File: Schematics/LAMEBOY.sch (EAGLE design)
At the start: 58 parts, among them IC1 PCF8574T, IC3 MCP73831, Q1 12MHz, U1 USD-SOCKETMICROSDEBAY, U2 USB

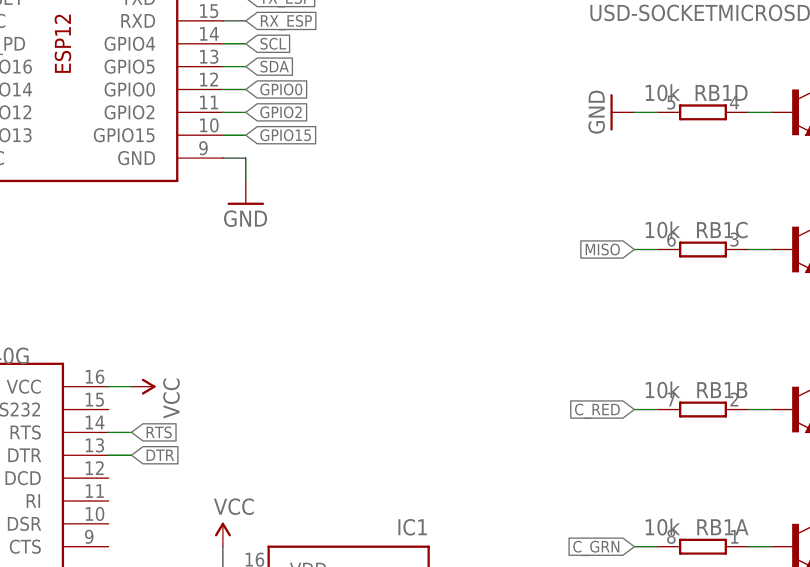
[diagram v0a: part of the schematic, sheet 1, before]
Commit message: bigger better resistor and crystal footprint
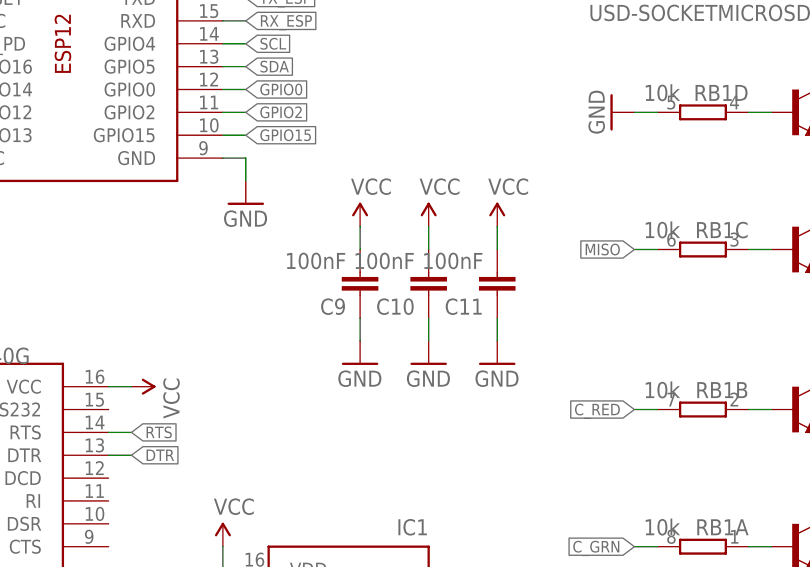
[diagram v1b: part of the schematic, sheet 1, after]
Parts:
- added C10, C11, C9: 100nF, rcl:C-EUONEFITSALL
- C1, C2, C3, C4, C5, C6, C7, C8: device rcl:C-EUC0603K -> rcl:C-EUONEFITSALL
- Q1: device adafruit:XTAL-4-3225 -> adafruit:XTAL-4BIGGER
- R1, R10, R11, R12, R13, R2, R3, R4, R5, R6, R7, R8, R9: device rcl:R-EU_R0603 -> rcl:R-EU_ONEFITSALL
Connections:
- net VREG_OUT renamed VREG_EN
- net GND: now also C10.1, C11.1, C9.1
- net VCC: now also C10.2, C11.2, C9.2
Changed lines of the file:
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@@
 <parts>
 <part name="U$1" library="lph-7366" deviceset="LPH-7366-SLOTS" device=""/>
-<part name="C1" library="rcl" deviceset="C-EU" device="C0603K" value="1uF"/>
+<part name="C1" library="rcl" deviceset="C-EU" device="ONEFITSALL" value="1uF"/>
 <part name="GND1" library="supply1" deviceset="GND" device=""/>
 <part name="LED1" library="led" deviceset="GM1WA55311A" device=""/>
@@
 <part name="LED3" library="led" deviceset="GM1WA55311A" device=""/>
 <part name="LED4" library="led" deviceset="GM1WA55311A" device=""/>
-<part name="C2" library="rcl" deviceset="C-EU" device="C0603K" value="1uF"/>
-<part name="C3" library="rcl" deviceset="C-EU" device="C0603K" value="1uF"/>
-<part name="C4" library="rcl" deviceset="C-EU" device="C0603K" value="1uF"/>
+<part name="C2" library="rcl" deviceset="C-EU" device="ONEFITSALL" value="1uF"/>
+<part name="C3" library="rcl" deviceset="C-EU" device="ONEFITSALL" value="1uF"/>
+<part name="C4" library="rcl" deviceset="C-EU" device="ONEFITSALL" value="1uF"/>
 <part name="GND2" library="supply1" deviceset="GND" device=""/>
 <part name="X1" library="adafruit" deviceset="ESP-12" device=""/>
@@
 <part name="SUPPLY3" library="SparkFun-Aesthetics" deviceset="VCC" device=""/>
 <part name="GND5" library="supply1" deviceset="GND" device=""/>
-<part name="R1" library="rcl" deviceset="R-EU_" device="R0603" value="10k"/>
+<part name="R1" library="rcl" deviceset="R-EU_" device="ONEFITSALL" value="10k"/>
 <part name="CH340G" library="ch340g" deviceset="CH340G" device="CH340G"/>
 <part name="IC1" library="micro-philips" deviceset="PCF8574" device="T" value="PCF8574T"/>
@@
 <part name="GND10" library="supply1" deviceset="GND" device=""/>
 <part name="GND11" library="supply1" deviceset="GND" device=""/>
-<part name="Q1" library="adafruit" deviceset="XTAL-4" device="-3225" value="12MHz"/>
-<part name="C5" library="rcl" deviceset="C-EU" device="C0603K" value="22pF"/>
-<part name="C6" library="rcl" deviceset="C-EU" device="C0603K" value="22pF"/>
-<part name="R2" library="rcl" deviceset="R-EU_" device="R0603" value="470"/>
-<part name="R3" library="rcl" deviceset="R-EU_" device="R0603" value="470"/>
+<part name="Q1" library="adafruit" deviceset="XTAL-4" device="BIGGER" value="12MHz"/>
+<part name="C5" library="rcl" deviceset="C-EU" device="ONEFITSALL" value="22pF"/>
+<part name="C6" library="rcl" deviceset="C-EU" device="ONEFITSALL" value="22pF"/>
+<part name="R2" library="rcl" deviceset="R-EU_" device="ONEFITSALL" value="470"/>
+<part name="R3" library="rcl" deviceset="R-EU_" device="ONEFITSALL" value="470"/>
 <part name="U$3" library="SparkFun-DiscreteSemi" deviceset="MMDT3904" device="" value="BC847S"/>
-<part name="R4" library="rcl" deviceset="R-EU_" device="R0603" value="4k7"/>
-<part name="R5" library="rcl" deviceset="R-EU_" device="R0603" value="4k7"/>
+<part name="R4" library="rcl" deviceset="R-EU_" device="ONEFITSALL" value="4k7"/>
+<part name="R5" library="rcl" deviceset="R-EU_" device="ONEFITSALL" value="4k7"/>
 <part name="SW_RST" library="SparkFun-Electromechanical" deviceset="SWITCH-MOMENTARY-2" device="-SMD-1101NE" value=""/>
 <part name="J1" library="SparkFun-Connectors" deviceset="JST_2MM_MALE" device=""/>
@@
 <part name="RPU" library="resistor-dil" deviceset="4R-N" device="0603-ARC" value="10k"/>
 <part name="SUPPLY9" library="SparkFun-Aesthetics" deviceset="VCC" device=""/>
-<part name="R6" library="rcl" deviceset="R-EU_" device="R0603" value="330k"/>
-<part name="R7" library="rcl" deviceset="R-EU_" device="R0603" value="100k"/>
+<part name="R6" library="rcl" deviceset="R-EU_" device="ONEFITSALL" value="330k"/>
+<part name="R7" library="rcl" deviceset="R-EU_" device="ONEFITSALL" value="100k"/>
 <part name="SUPPLY10" library="SparkFun-Aesthetics" deviceset="VCC" device=""/>
 <part name="GND14" library="supply1" deviceset="GND" device=""/>
 <part name="GND15" library="supply1" deviceset="GND" device=""/>
 <part name="S2" library="SparkFun-Electromechanical" deviceset="SWITCH-SPDT" device="-SMD-A" value="PWR"/>
-<part name="R8" library="rcl" deviceset="R-EU_" device="R0603" value="10k"/>
+<part name="R8" library="rcl" deviceset="R-EU_" device="ONEFITSALL" value="10k"/>
 <part name="GND16" library="supply1" deviceset="GND" device=""/>
 <part name="GND17" library="supply1" deviceset="GND" device=""/>
@@
 <part name="IC3" library="adafruit" deviceset="MCP73831" device="/OT" value="MCP73831"/>
 <part name="CHARGE" library="led" deviceset="LED" device="CHIP-LED0805"/>
-<part name="R9" library="rcl" deviceset="R-EU_" device="R0603" value="470"/>
-<part name="C7" library="rcl" deviceset="C-EU" device="C0603K" value="4.7uF"/>
-<part name="C8" library="rcl" deviceset="C-EU" device="C0603K" value="4.7uF"/>
+<part name="R9" library="rcl" deviceset="R-EU_" device="ONEFITSALL" value="470"/>
+<part name="C7" library="rcl" deviceset="C-EU" device="ONEFITSALL" value="4.7uF"/>
+<part name="C8" library="rcl" deviceset="C-EU" device="ONEFITSALL" value="4.7uF"/>
 <part name="GND18" library="supply1" deviceset="GND" device=""/>
 <part name="GND19" library="supply1" deviceset="GND" device=""/>
-<part name="R10" library="rcl" deviceset="R-EU_" device="R0603" value="2k"/>
+<part name="R10" library="rcl" deviceset="R-EU_" device="ONEFITSALL" value="2k"/>
 <part name="GND20" library="supply1" deviceset="GND" device=""/>
 <part name="U$4" library="TPS2113" deviceset="TPS2113-PW" device=""/>
 <part name="GND21" library="supply1" deviceset="GND" device=""/>
-<part name="R11" library="rcl" deviceset="R-EU_" device="R0603" value="470"/>
+<part name="R11" library="rcl" deviceset="R-EU_" device="ONEFITSALL" value="470"/>
 <part name="GND22" library="supply1" deviceset="GND" device=""/>
 <part name="SUPPLY1" library="SparkFun-Aesthetics" deviceset="VCC" device=""/>
@@
 <part name="GND25" library="supply1" deviceset="GND" device=""/>
 <part name="GND26" library="supply1" deviceset="GND" device=""/>
-<part name="R12" library="rcl" deviceset="R-EU_" device="R0603" value="10k"/>
-<part name="R13" library="rcl" deviceset="R-EU_" device="R0603" value="10k"/>
+<part name="R12" library="rcl" deviceset="R-EU_" device="ONEFITSALL" value="10k"/>
+<part name="R13" library="rcl" deviceset="R-EU_" device="ONEFITSALL" value="10k"/>
 <part name="SUPPLY12" library="SparkFun-Aesthetics" deviceset="VCC" device=""/>
 <part name="GND27" library="supply1" deviceset="GND" device=""/>
@@
 <part name="S7" library="SparkFun-Electromechanical" deviceset="SWITCH-MOMENTARY-2" device="SMD-4"/>
 <part name="S8" library="SparkFun-Electromechanical" deviceset="SWITCH-MOMENTARY-2" device="SMD-4"/>
+<part name="C9" library="rcl" deviceset="C-EU" device="ONEFITSALL" value="100nF"/>
+<part name="GND12" library="supply1" deviceset="GND" device=""/>
+<part name="SUPPLY4" library="SparkFun-Aesthetics" deviceset="VCC" device=""/>
+<part name="C10" library="rcl" deviceset="C-EU" device="ONEFITSALL" value="100nF"/>
+<part name="GND36" library="supply1" deviceset="GND" device=""/>
+<part name="SUPPLY7" library="SparkFun-Aesthetics" deviceset="VCC" device=""/>
+<part name="C11" library="rcl" deviceset="C-EU" device="ONEFITSALL" value="100nF"/>
+<part name="GND37" library="supply1" deviceset="GND" device=""/>
+<part name="SUPPLY11" library="SparkFun-Aesthetics" deviceset="VCC" device=""/>
 </parts>
 <sheets>
@@
 <attribute name="NAME" x="53.34" y="71.12" size="1.778" layer="95"/>
 </instance>
+<instance part="C9" gate="G$1" x="144.78" y="68.58" rot="R180"/>
+<instance part="GND12" gate="1" x="144.78" y="60.96"/>
+<instance part="SUPPLY4" gate="G$1" x="144.78" y="76.2"/>
+<instance part="C10" gate="G$1" x="152.4" y="68.58" rot="R180"/>
+<instance part="GND36" gate="1" x="152.4" y="60.96"/>
+<instance part="SUPPLY7" gate="G$1" x="152.4" y="76.2"/>
+<instance part="C11" gate="G$1" x="160.02" y="68.58" rot="R180"/>
+<instance part="GND37" gate="1" x="160.02" y="60.96"/>
+<instance part="SUPPLY11" gate="G$1" x="160.02" y="76.2"/>
 </instances>
 <busses>
@@
 <pinref part="GND33" gate="1" pin="GND"/>
 </segment>
+<segment>
+<pinref part="C9" gate="G$1" pin="1"/>
+<pinref part="GND12" gate="1" pin="GND"/>
+<wire x1="144.78" y1="66.04" x2="144.78" y2="63.5" width="0.1524" layer="91"/>
+</segment>
+<segment>
+<pinref part="C10" gate="G$1" pin="1"/>
+<pinref part="GND36" gate="1" pin="GND"/>
+<wire x1="152.4" y1="66.04" x2="152.4" y2="63.5" width="0.1524" layer="91"/>
+</segment>
+<segment>
+<pinref part="C11" gate="G$1" pin="1"/>
+<pinref part="GND37" gate="1" pin="GND"/>
+<wire x1="160.02" y1="66.04" x2="160.02" y2="63.5" width="0.1524" layer="91"/>
+</segment>
 </net>
 <net name="VCC" class="0">
@@
 <pinref part="SUPPLY13" gate="G$1" pin="VCC"/>
 <wire x1="157.48" y1="127" x2="165.1" y2="127" width="0.1524" layer="91"/>
+</segment>
+<segment>
+<pinref part="C9" gate="G$1" pin="2"/>
+<pinref part="SUPPLY4" gate="G$1" pin="VCC"/>
+<wire x1="144.78" y1="76.2" x2="144.78" y2="73.66" width="0.1524" layer="91"/>
+</segment>
+<segment>
+<pinref part="C10" gate="G$1" pin="2"/>
+<pinref part="SUPPLY7" gate="G$1" pin="VCC"/>
+<wire x1="152.4" y1="76.2" x2="152.4" y2="73.66" width="0.1524" layer="91"/>
+</segment>
+<segment>
+<pinref part="C11" gate="G$1" pin="2"/>
+<pinref part="SUPPLY11" gate="G$1" pin="VCC"/>
+<wire x1="160.02" y1="76.2" x2="160.02" y2="73.66" width="0.1524" layer="91"/>
 </segment>
 </net>
@@
 </segment>
 </net>
-<net name="VREG_OUT" class="0">
+<net name="VREG_EN" class="0">
 <segment>
 <pinref part="S2" gate="1" pin="P"/>

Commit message: corrected rgb layout
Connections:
- net N$1 renamed BLUE_LED
- removed net N$2: LED4.CBLUE, RRD.1
- removed net N$3: LED4.CRED, RGD.1
- new net GREEN_LED: LED4.CBLUE, RGD.1
- new net RED_LED: LED4.CRED, RRD.1
- net C_GRN: now also RB1B.2; no longer RB1A.2
- net C_RED: now also RB1A.2; no longer RB1B.2
- net GRN: now also U$6G$2.C; no longer U$6G$1.C
- net L2_R: now also RGA.1; no longer RRA.1
- net L4_G: now also RRA.1; no longer RGA.1
- net N$10: now also RRB.1; no longer RGB.1
- net N$5: now also RGC.1; no longer RRC.1
- net N$6: now also RRC.1; no longer RGC.1
- net N$9: now also RGB.1; no longer RRB.1
- net RED: now also U$6G$1.C; no longer U$6G$2.C
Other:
- moved on the sheet: RGA, RGB, RGC, RGD, RRA, RRB, RRC, RRD
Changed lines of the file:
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@@
 <part name="X1" library="adafruit" deviceset="ESP-12" device=""/>
 <part name="RB" library="resistor-dil" deviceset="4R-N" device="0603-ARC" value="150"/>
+<part name="RG" library="resistor-dil" deviceset="4R-N" device="0603-ARC" value="150"/>
 <part name="RR" library="resistor-dil" deviceset="4R-N" device="0603-ARC" value="100"/>
-<part name="RG" library="resistor-dil" deviceset="4R-N" device="0603-ARC" value="150"/>
 <part name="U$2" library="SparkFun-DigitalIC" deviceset="ATTINY13" device="SO08-WIDE" value="ATTINY13SO08-WIDE"/>
 <part name="JP2" library="SparkFun-Connectors" deviceset="AVR_SPI_PRG_6" device=""/>
@@
 <instance part="RB" gate="C" x="116.84" y="142.24" rot="R90"/>
 <instance part="RB" gate="D" x="132.08" y="142.24" rot="R90"/>
-<instance part="RR" gate="A" x="91.44" y="142.24" rot="R90"/>
-<instance part="RR" gate="B" x="106.68" y="142.24" rot="R90"/>
-<instance part="RR" gate="C" x="121.92" y="142.24" rot="R90"/>
-<instance part="RR" gate="D" x="137.16" y="142.24" rot="R90"/>
-<instance part="RG" gate="A" x="96.52" y="142.24" rot="R90"/>
-<instance part="RG" gate="B" x="111.76" y="142.24" rot="R90"/>
-<instance part="RG" gate="C" x="127" y="142.24" rot="R90"/>
-<instance part="RG" gate="D" x="142.24" y="142.24" rot="R90"/>
+<instance part="RG" gate="A" x="91.44" y="142.24" rot="R90"/>
+<instance part="RG" gate="B" x="106.68" y="142.24" rot="R90"/>
+<instance part="RG" gate="C" x="121.92" y="142.24" rot="R90"/>
+<instance part="RG" gate="D" x="137.16" y="142.24" rot="R90"/>
+<instance part="RR" gate="A" x="96.52" y="142.24" rot="R90"/>
+<instance part="RR" gate="B" x="111.76" y="142.24" rot="R90"/>
+<instance part="RR" gate="C" x="127" y="142.24" rot="R90"/>
+<instance part="RR" gate="D" x="142.24" y="142.24" rot="R90"/>
 <instance part="U$2" gate="G$1" x="53.34" y="134.62"/>
 <instance part="JP2" gate="G$1" x="172.72" y="149.86"/>
@@
 </segment>
 </net>
-<net name="N$1" class="0">
+<net name="BLUE_LED" class="0">
 <segment>
 <pinref part="RB" gate="D" pin="1"/>
@@
 </segment>
 </net>
-<net name="N$2" class="0">
-<segment>
-<pinref part="RR" gate="D" pin="1"/>
+<net name="GREEN_LED" class="0">
+<segment>
+<pinref part="RG" gate="D" pin="1"/>
 <wire x1="137.16" y1="132.08" x2="137.16" y2="137.16" width="0.1524" layer="91"/>
 <pinref part="LED4" gate="G$1" pin="CBLUE"/>
 </segment>
 </net>
-<net name="N$3" class="0">
-<segment>
-<pinref part="RG" gate="D" pin="1"/>
+<net name="RED_LED" class="0">
+<segment>
+<pinref part="RR" gate="D" pin="1"/>
 <wire x1="142.24" y1="132.08" x2="142.24" y2="137.16" width="0.1524" layer="91"/>
 <pinref part="LED4" gate="G$1" pin="CRED"/>
@@
 <net name="N$5" class="0">
 <segment>
-<pinref part="RR" gate="C" pin="1"/>
+<pinref part="RG" gate="C" pin="1"/>
 <wire x1="121.92" y1="132.08" x2="121.92" y2="137.16" width="0.1524" layer="91"/>
 <pinref part="LED3" gate="G$1" pin="CBLUE"/>
@@
 <net name="N$6" class="0">
 <segment>
-<pinref part="RG" gate="C" pin="1"/>
+<pinref part="RR" gate="C" pin="1"/>
 <wire x1="127" y1="132.08" x2="127" y2="137.16" width="0.1524" layer="91"/>
 <pinref part="LED3" gate="G$1" pin="CRED"/>
@@
 <net name="N$9" class="0">
 <segment>
-<pinref part="RR" gate="B" pin="1"/>
+<pinref part="RG" gate="B" pin="1"/>
 <wire x1="106.68" y1="132.08" x2="106.68" y2="137.16" width="0.1524" layer="91"/>
 <pinref part="LED2" gate="G$1" pin="CBLUE"/>
@@
 <net name="N$10" class="0">
 <segment>
-<pinref part="RG" gate="B" pin="1"/>
+<pinref part="RR" gate="B" pin="1"/>
 <wire x1="111.76" y1="132.08" x2="111.76" y2="137.16" width="0.1524" layer="91"/>
 <pinref part="LED2" gate="G$1" pin="CRED"/>
@@
 <net name="L2_R" class="0">
 <segment>
-<pinref part="RR" gate="A" pin="1"/>
+<pinref part="RG" gate="A" pin="1"/>
 <wire x1="91.44" y1="132.08" x2="91.44" y2="137.16" width="0.1524" layer="91"/>
 <pinref part="LED1" gate="G$1" pin="CBLUE"/>
@@
 <net name="L4_G" class="0">
 <segment>
-<pinref part="RG" gate="A" pin="1"/>
+<pinref part="RR" gate="A" pin="1"/>
 <wire x1="96.52" y1="132.08" x2="96.52" y2="137.16" width="0.1524" layer="91"/>
 <pinref part="LED1" gate="G$1" pin="CRED"/>
@@
 </segment>
 <segment>
+<pinref part="RB1" gate="B" pin="2"/>
+<wire x1="177.8" y1="55.88" x2="175.26" y2="55.88" width="0.1524" layer="91"/>
+<label x="175.26" y="55.88" size="1.27" layer="95" rot="R180" xref="yes"/>
+</segment>
+</net>
+<net name="MISO" class="0">
+<segment>
+<pinref part="U$2" gate="G$1" pin="PB1(MISO)"/>
+<wire x1="66.04" y1="139.7" x2="68.58" y2="139.7" width="0.1524" layer="91"/>
+<label x="68.58" y="139.7" size="1.27" layer="95" xref="yes"/>
+</segment>
+<segment>
+<pinref part="JP2" gate="G$1" pin="1"/>
+<wire x1="165.1" y1="152.4" x2="160.02" y2="152.4" width="0.1524" layer="91"/>
+<label x="160.02" y="152.4" size="1.27" layer="95" rot="R180" xref="yes"/>
+</segment>
+<segment>
+<pinref part="RB1" gate="C" pin="2"/>
+<wire x1="177.8" y1="73.66" x2="175.26" y2="73.66" width="0.1524" layer="91"/>
+<label x="175.26" y="73.66" size="1.27" layer="95" rot="R180" xref="yes"/>
+</segment>
+</net>
+<net name="C_RED" class="0">
+<segment>
+<pinref part="U$2" gate="G$1" pin="PB4(ADC2)"/>
+<wire x1="66.04" y1="132.08" x2="68.58" y2="132.08" width="0.1524" layer="91"/>
+<label x="68.58" y="132.08" size="1.27" layer="95" xref="yes"/>
+</segment>
+<segment>
 <pinref part="RB1" gate="A" pin="2"/>
 <wire x1="177.8" y1="40.64" x2="175.26" y2="40.64" width="0.1524" layer="91"/>
 <label x="175.26" y="40.64" size="1.27" layer="95" rot="R180" xref="yes"/>
-</segment>
-</net>
-<net name="MISO" class="0">
-<segment>
-<pinref part="U$2" gate="G$1" pin="PB1(MISO)"/>
-<wire x1="66.04" y1="139.7" x2="68.58" y2="139.7" width="0.1524" layer="91"/>
-<label x="68.58" y="139.7" size="1.27" layer="95" xref="yes"/>
-</segment>
-<segment>
-<pinref part="JP2" gate="G$1" pin="1"/>
-<wire x1="165.1" y1="152.4" x2="160.02" y2="152.4" width="0.1524" layer="91"/>
-<label x="160.02" y="152.4" size="1.27" layer="95" rot="R180" xref="yes"/>
-</segment>
-<segment>
-<pinref part="RB1" gate="C" pin="2"/>
-<wire x1="177.8" y1="73.66" x2="175.26" y2="73.66" width="0.1524" layer="91"/>
-<label x="175.26" y="73.66" size="1.27" layer="95" rot="R180" xref="yes"/>
-</segment>
-</net>
-<net name="C_RED" class="0">
-<segment>
-<pinref part="U$2" gate="G$1" pin="PB4(ADC2)"/>
-<wire x1="66.04" y1="132.08" x2="68.58" y2="132.08" width="0.1524" layer="91"/>
-<label x="68.58" y="132.08" size="1.27" layer="95" xref="yes"/>
-</segment>
-<segment>
-<pinref part="RB1" gate="B" pin="2"/>
-<wire x1="177.8" y1="55.88" x2="175.26" y2="55.88" width="0.1524" layer="91"/>
-<label x="175.26" y="55.88" size="1.27" layer="95" rot="R180" xref="yes"/>
 </segment>
 </net>
@@
 </segment>
 </net>
-<net name="GRN" class="0">
-<segment>
-<pinref part="RG" gate="A" pin="2"/>
+<net name="RED" class="0">
+<segment>
+<pinref part="RR" gate="A" pin="2"/>
 <wire x1="96.52" y1="147.32" x2="96.52" y2="154.94" width="0.1524" layer="91"/>
-<pinref part="RG" gate="B" pin="2"/>
+<pinref part="RR" gate="B" pin="2"/>
 <wire x1="96.52" y1="154.94" x2="111.76" y2="154.94" width="0.1524" layer="91"/>
 <wire x1="111.76" y1="147.32" x2="111.76" y2="154.94" width="0.1524" layer="91"/>
-<pinref part="RG" gate="C" pin="2"/>
+<pinref part="RR" gate="C" pin="2"/>
 <wire x1="111.76" y1="154.94" x2="127" y2="154.94" width="0.1524" layer="91"/>
 <wire x1="127" y1="147.32" x2="127" y2="154.94" width="0.1524" layer="91"/>
-<pinref part="RG" gate="D" pin="2"/>
+<pinref part="RR" gate="D" pin="2"/>
 <wire x1="127" y1="154.94" x2="142.24" y2="154.94" width="0.1524" layer="91"/>
 <wire x1="142.24" y1="154.94" x2="142.24" y2="147.32" width="0.1524" layer="91"/>
@@
 </segment>
 </net>
-<net name="RED" class="0">
-<segment>
-<pinref part="RR" gate="A" pin="2"/>
+<net name="GRN" class="0">
+<segment>
+<pinref part="RG" gate="A" pin="2"/>
 <wire x1="91.44" y1="147.32" x2="91.44" y2="152.4" width="0.1524" layer="91"/>
-<pinref part="RR" gate="B" pin="2"/>
+<pinref part="RG" gate="B" pin="2"/>
 <wire x1="91.44" y1="152.4" x2="106.68" y2="152.4" width="0.1524" layer="91"/>
 <wire x1="106.68" y1="147.32" x2="106.68" y2="152.4" width="0.1524" layer="91"/>
-<pinref part="RR" gate="C" pin="2"/>
+<pinref part="RG" gate="C" pin="2"/>
 <wire x1="106.68" y1="152.4" x2="121.92" y2="152.4" width="0.1524" layer="91"/>
 <wire x1="121.92" y1="147.32" x2="121.92" y2="152.4" width="0.1524" layer="91"/>
-<pinref part="RR" gate="D" pin="2"/>
+<pinref part="RG" gate="D" pin="2"/>
 <wire x1="121.92" y1="152.4" x2="137.16" y2="152.4" width="0.1524" layer="91"/>
 <wire x1="137.16" y1="152.4" x2="137.16" y2="147.32" width="0.1524" layer="91"/>

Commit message: moved C and RST switch
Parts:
- CHARGE: device led:LEDCHIP-LED0805 -> led:LEDCHARLIE
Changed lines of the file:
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@@
 <part name="F1" library="SparkFun-PowerIC" deviceset="PTC" device="SMD"/>
 <part name="IC3" library="adafruit" deviceset="MCP73831" device="/OT" value="MCP73831"/>
-<part name="CHARGE" library="led" deviceset="LED" device="CHIP-LED0805"/>
+<part name="CHARGE" library="led" deviceset="LED" device="CHARLIE"/>
 <part name="R9" library="rcl" deviceset="R-EU_" device="ONEFITSALL" value="470"/>
 <part name="C7" library="rcl" deviceset="C-EU" device="ONEFITSALL" value="4.7uF"/>
